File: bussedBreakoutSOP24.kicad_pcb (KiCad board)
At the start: 2 copper layers, 2.9 x 2.9 mm, 46 parts, among them J1 Conn_01x12_Pin, J10 Conn_01x06_Pin, J11 Conn_01x06_Pin, J12 Conn_01x06_Pin, J13 Conn_01x06_Pin, J14 Conn_01x06_Pin, J15 Conn_01x06_Pin, J16 Conn_01x06_Pin, J17 Conn_01x06_Pin, J18 Conn_01x06_Pin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

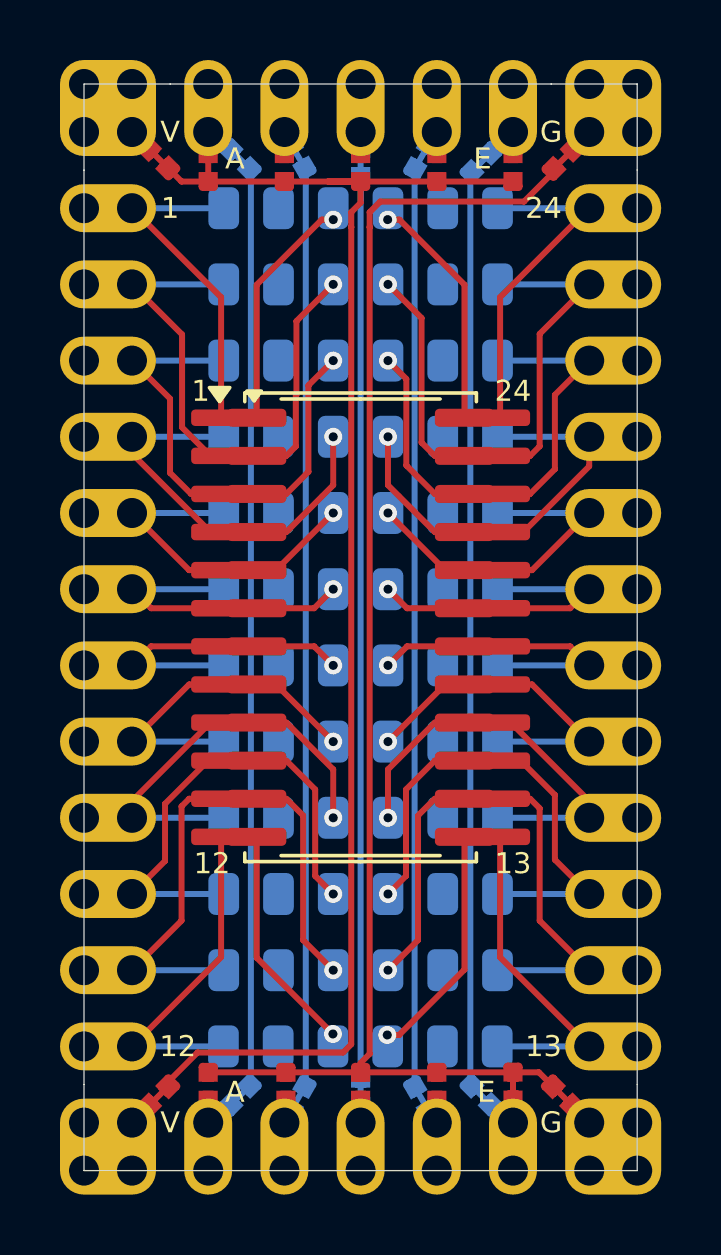
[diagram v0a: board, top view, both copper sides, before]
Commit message: Change to a custom SOP-24 footprint accomodating the narrowest 3.9mm to the widest 7.5mm SO-24 packages
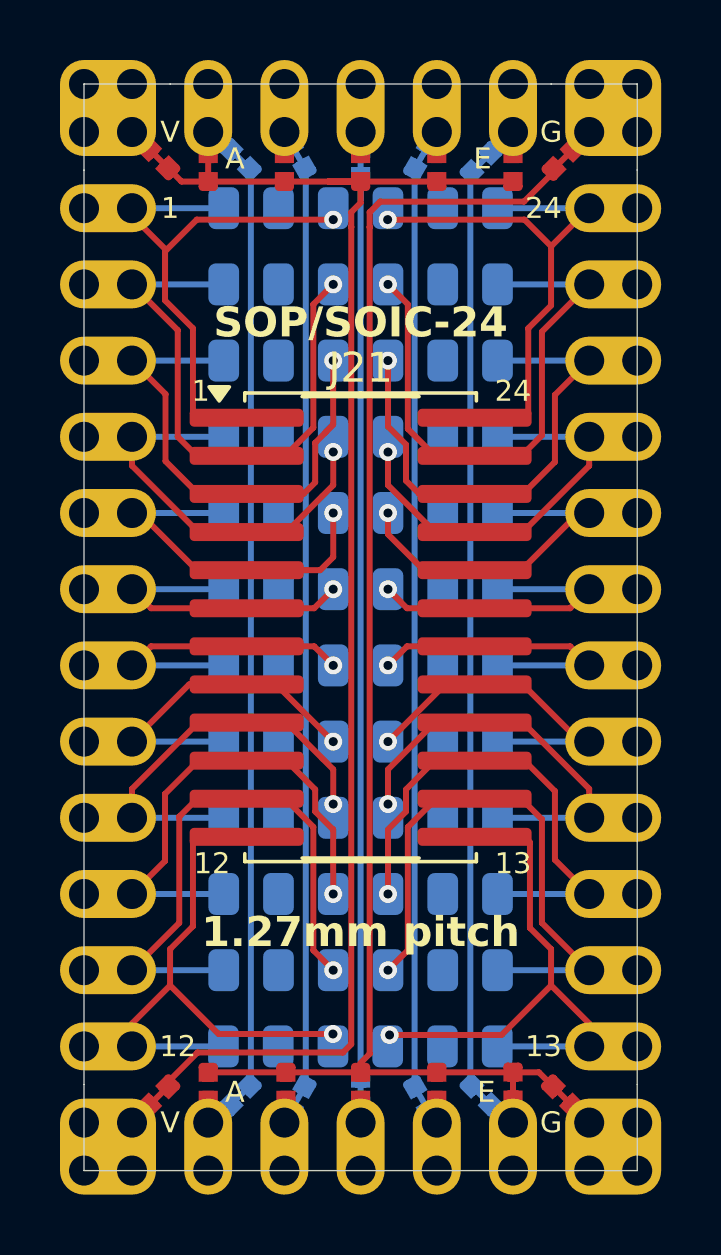
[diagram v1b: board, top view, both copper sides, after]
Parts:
- removed J22: 5.3mm SOP-24, Package_SO:SO-24_5.3x15mm_P1.27mm
- J21: value 7.5mm SOP-24 -> SOP-24; footprint Package_SO:SOP-24_7.5x15.4mm_P1.27mm -> SMD:SOP-24_3.9-7.5mmx15.4mm_P1.27mm
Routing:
- net /3: track 15.4 -> 16.9 mm
- net /5: track 10.2 -> 11.0 mm
- net /1: track 19.2 -> 18.4 mm
- net /24: track 19.2 -> 18.4 mm
- net /21: track 12.7 -> 12.2 mm
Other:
- board text added: "1.27mm pitch"
- board text added: "NC"
- board text added: "SOP/SOIC-24"
